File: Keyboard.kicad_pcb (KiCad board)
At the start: 2 copper layers, 231.8 x 98.9 mm, 153 parts, among them Q1 BSS138, Q2 BSS138, SW1 SW_Kailh_1u, SW10 SW_Kailh_1u, SW11 SW_Kailh_1u, SW12 SW_Kailh_1u, SW13 SW_Kailh_1u, SW14 SW_Kailh_1u, SW15 SW_Kailh_1u, SW16 SW_Kailh_1u, SW17 SW_Kailh_1u, SW18 SW_Kailh_1u, SW19 SW_Kailh_1u, SW2 SW_Kailh_1u, SW20 SW_Kailh_1u, SW21 SW_Kailh_1u, SW22 SW_Kailh_1u, SW23 SW_Kailh_1u, SW23_3u1 SW_Kailh_3u, SW24 SW_Kailh_1u, SW25 SW_Kailh_1u, SW26 SW_Kailh_1u, SW27 SW_Kailh_1u, SW28 SW_Kailh_1u, SW29 SW_Kailh_1u, SW3 SW_Kailh_1u, SW30 SW_Kailh_1u, SW31 SW_Kailh_1u, SW32 SW_Kailh_1u, SW33 SW_Kailh_1u, SW34 SW_Kailh_1u, SW35 SW_Kailh_1u, SW36 SW_Kailh_1u, SW37 SW_Kailh_1u, SW38 SW_Kailh_1u, SW39 SW_Kailh_1u, SW4 SW_Kailh_1u, SW40 SW_Kailh_1u, SW41 SW_Kailh_1u, SW42 SW_Kailh_1u, SW43 SW_Kailh_1u, SW44 SW_Kailh_1u, SW45 SW_Kailh_1u, SW5 SW_Kailh_1u, SW6 SW_Kailh_1u, SW7 SW_Kailh_1u, SW8 SW_Kailh_1u, SW9 SW_Kailh_1u, U1 PCAL6416APW, U2 Seeed Studio XIAO SAMD21, U3 NSI50350ADT4G

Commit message: rev 1.2
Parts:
- D1, D10, D11, D12, D13, D14, D15, D16, D17, D18, D19, D2, D20, D21, D22, D23, D24, D25, D26, D27, D28, D29, D3, D30, D31, D32, D33, D34, D35, D36, D37, D38, D39, D4, D40, D41, D42, D43, D44, D45, D46, D5, D6, D7, D8, D9: value 1N4148 -> 1N4148W; footprint Diode_SMD:D_1206_3216Metric_Pad1.42x1.75mm_HandSolder -> Diode_SMD:D_SOD-123
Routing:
- added copper zone on B.Cu, net GND
- added copper zone on F.Cu, net GND

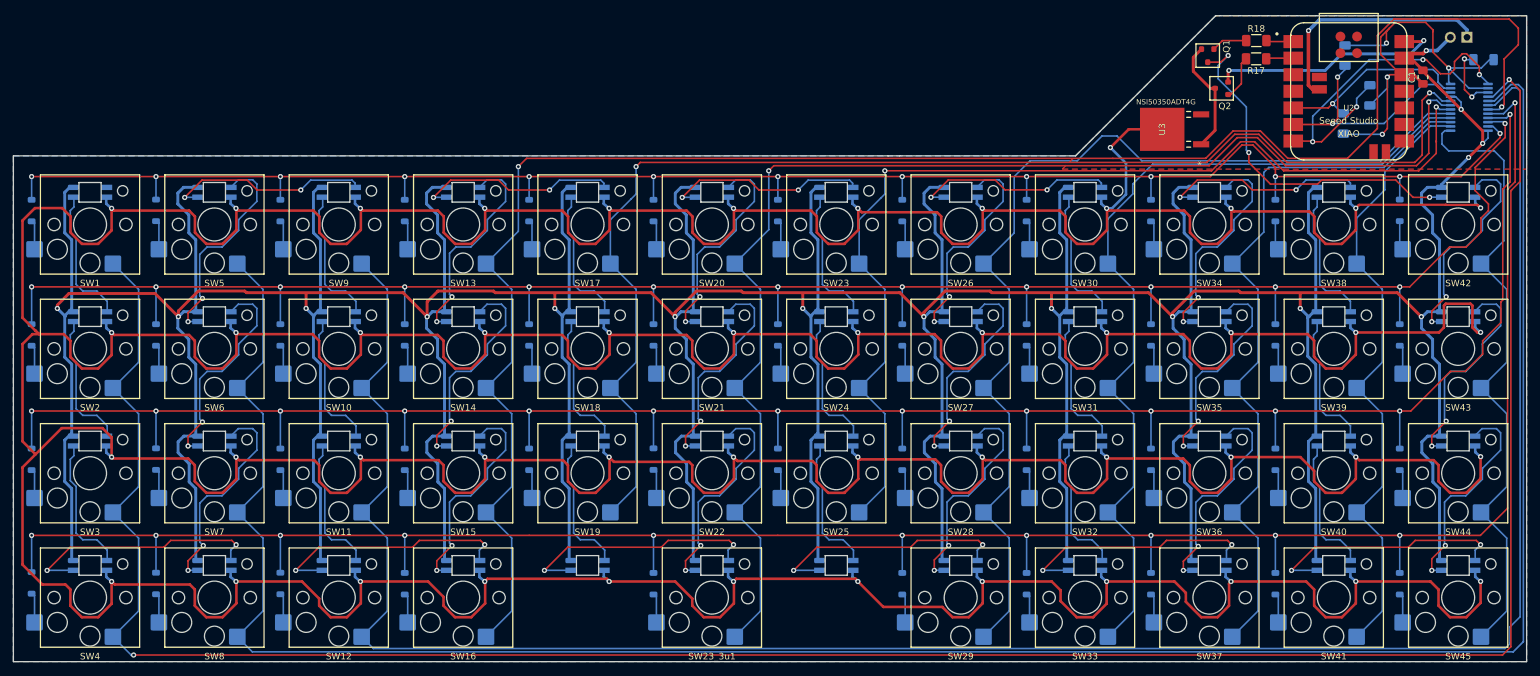
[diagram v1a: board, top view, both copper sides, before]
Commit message: rounded corners, replaced current reg with fuse
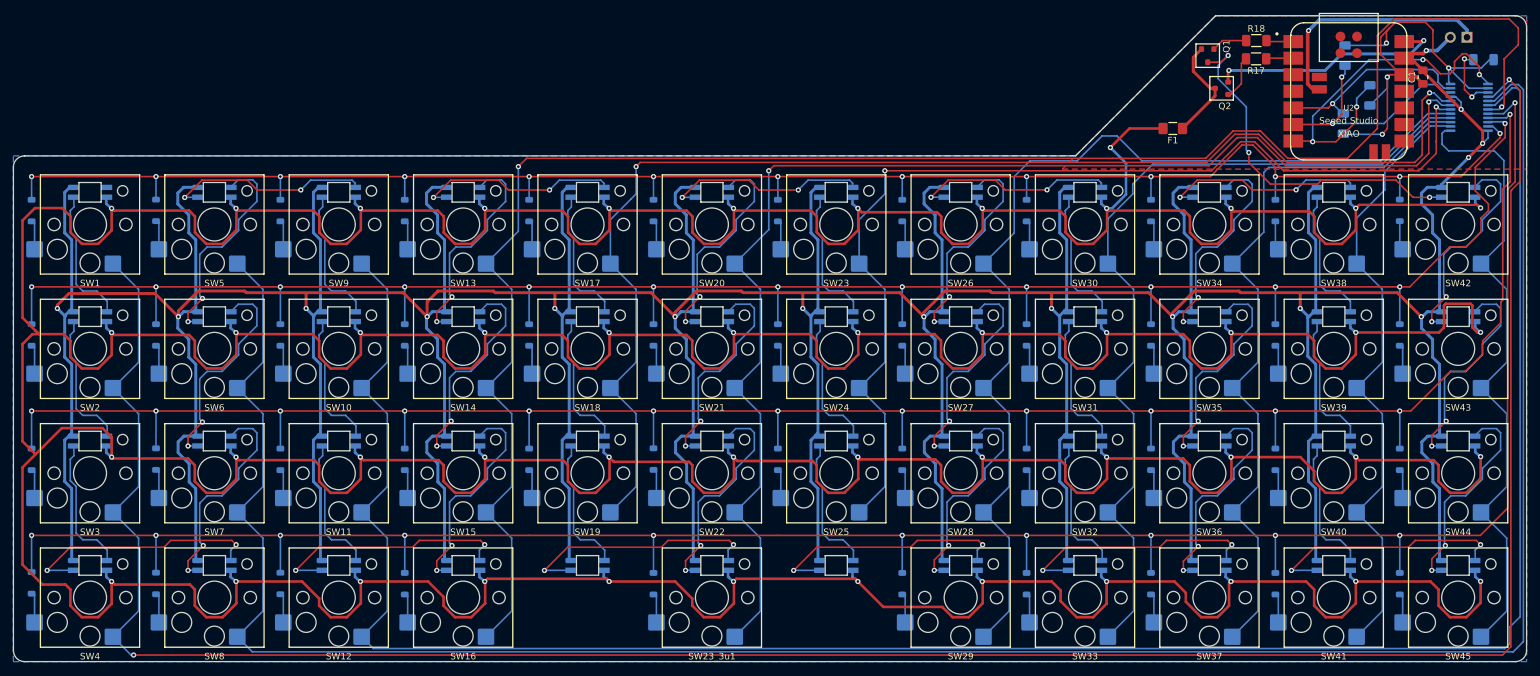
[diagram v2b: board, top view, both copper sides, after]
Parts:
- removed U3: NSI50350ADT4G, footprints:NSI50350ADT4G
- added F1: 500mA, Fuse:Fuse_1206_3216Metric_Pad1.42x1.75mm_HandSolder, F.Cu at (200.4, 55.5)
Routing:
- net INT: track 56.0 -> 57.3 mm
- net Net-(Q1-S): track 17.8 -> 16.6 mm
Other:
- outline, holes or cut-outs redrawn

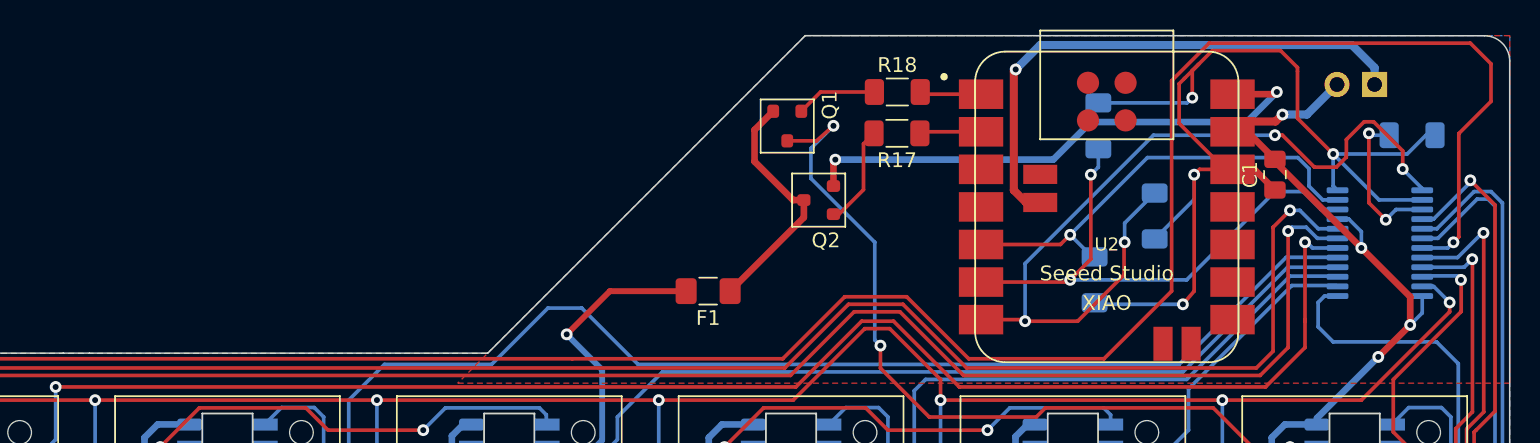
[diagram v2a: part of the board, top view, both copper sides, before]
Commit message: changed led mosfet and resistors
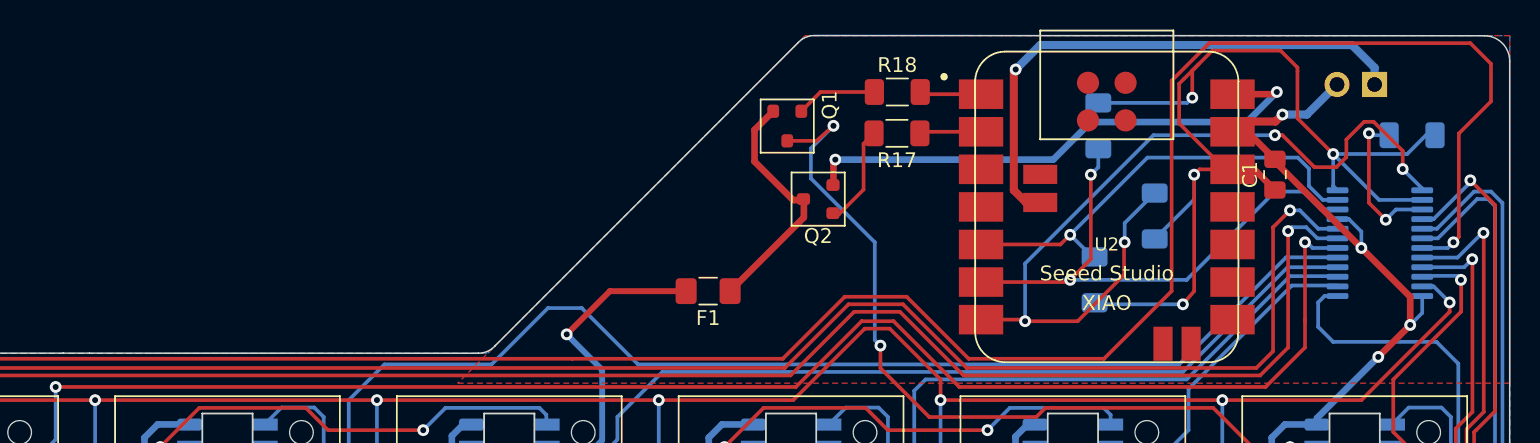
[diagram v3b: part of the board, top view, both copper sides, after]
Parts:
- Q2: value BSS138 -> DMG3402L
- R17, R18: value 10k -> 1k
- moved Q2 0.07 mm to (207.9, 49.3)
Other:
- outline, holes or cut-outs redrawn
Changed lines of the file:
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@@
         (effects (font (size 1 1) (thickness 0.15)))
     )
-    (fp_text value "10k" (at 0 1.82) (layer "F.Fab")
+    (fp_text value "1k" (at 0 1.82) (layer "F.Fab")
         (effects (font (size 1 1) (thickness 0.15)))
     )
@@
       (net 1 "Net-(BT1-+)") (pinfunction "BAT+") (pintype "input"))
   )
+  (footprint "PCM_Package_TO_SOT_SMD_AKL:SOT-23" (layer "F.Cu")
+    (at 207.883 49.276 180)
+    (descr "SOT-23, Standard, Alternate KiCad Library")
+    (tags "SOT-23")
+    (property "Sheetfile" "rgb.kicad_sch")
+    (property "Sheetname" "RGB LEDs")
+    (property "ki_description" "SOT-23 N-MOSFET enchancement mode transistor, 30V, 4A, 1.4W, Alternate KiCAD Library")
+    (property "ki_keywords" "enchancement mosfet nmosfet n-mosfet nmos n-mos emos emosfet DMG3402L")
+    (attr smd)
+    (fp_text reference "Q2" (at 0 -2.5) (layer "F.SilkS")
+        (effects (font (size 1 1) (thickness 0.15)))
+    )
+    (fp_text value "DMG3402L" (at 0 2.5) (layer "F.Fab") hide
+        (effects (font (size 1 1) (thickness 0.15)))
+    )
+    (fp_text user "${REFERENCE}" (at 0 0 90) (layer "F.Fab")
+        (effects (font (size 0.5 0.5) (thickness 0.075)))
+    )
+    (fp_line (start -1.8 -1.8) (end -1.8 1.8)
+      (stroke (width 0.12) (type solid)) (layer "F.SilkS"))
+    (fp_line (start -1.8 1.8) (end 1.8 1.8)
+      (stroke (width 0.12) (type solid)) (layer "F.SilkS"))
+    (fp_line (start 1.8 -1.8) (end -1.8 -1.8)
+      (stroke (width 0.12) (type solid)) (layer "F.SilkS"))
+    (fp_line (start 1.8 1.8) (end 1.8 -1.8)
+      (stroke (width 0.12) (type solid)) (layer "F.SilkS"))
+    (fp_line (start -1.7 -1.75) (end 1.7 -1.75)
+      (stroke (width 0.05) (type solid)) (layer "F.CrtYd"))
+    (fp_line (start -1.7 1.75) (end -1.7 -1.75)
+      (stroke (width 0.05) (type solid)) (layer "F.CrtYd"))
+    (fp_line (start 1.7 -1.75) (end 1.7 1.75)
+      (stroke (width 0.05) (type solid)) (layer "F.CrtYd"))
+    (fp_line (start 1.7 1.75) (end -1.7 1.75)
+      (stroke (width 0.05) (type solid)) (layer "F.CrtYd"))
+    (fp_line (start -1.3 -1.2) (end -1.3 -0.7)
+      (stroke (width 0.1) (type solid)) (layer "F.Fab"))
+    (fp_line (start -1.3 -0.7) (end -0.7 -0.7)
+      (stroke (width 0.1) (type solid)) (layer "F.Fab"))
+    (fp_line (start -1.3 0.7) (end -1.3 1.2)
+      (stroke (width 0.1) (type solid)) (layer "F.Fab"))
+    (fp_line (start -1.3 1.2) (end -0.7 1.2)
+      (stroke (width 0.1) (type solid)) (layer "F.Fab"))
+    (fp_line (start -0.7 -1.52) (end -0.7 1.5)
+      (stroke (width 0.1) (type solid)) (layer "F.Fab"))
+    (fp_line (start -0.7 -1.52) (end 0.7 -1.52)
+      (stroke (width 0.1) (type solid)) (layer "F.Fab"))
+    (fp_line (start -0.7 -1.2) (end -1.3 -1.2)
+      (stroke (width 0.1) (type solid)) (layer "F.Fab"))
+    (fp_line (start -0.7 0.7) (end -1.3 0.7)
+      (stroke (width 0.1) (type solid)) (layer "F.Fab"))
+    (fp_line (start -0.7 1.52) (end 0.7 1.52)
+      (stroke (width 0.1) (type solid)) (layer "F.Fab"))
+    (fp_line (start 0.7 -1.52) (end 0.7 1.52)
+      (stroke (width 0.1) (type solid)) (layer "F.Fab"))
+    (fp_line (start 0.7 0.25) (end 1.3 0.25)
+      (stroke (width 0.1) (type solid)) (layer "F.Fab"))
+    (fp_line (start 1.3 -0.25) (end 0.7 -0.25)
+      (stroke (width 0.1) (type solid)) (layer "F.Fab"))
+    (fp_line (start 1.3 0.25) (end 1.3 -0.25)
+      (stroke (width 0.1) (type solid)) (layer "F.Fab"))
+    (pad "1" smd roundrect (at -1 -0.95 180) (size 0.9 0.8) (layers "F.Cu" "F.Paste" "F.Mask") (roundrect_rratio 0.25)
+      (net 134 "Net-(Q2-G)") (pinfunction "G") (pintype "input"))
+    (pad "2" smd roundrect (at -1 0.95 180) (size 0.9 0.8) (layers "F.Cu" "F.Paste" "F.Mask") (roundrect_rratio 0.25)
+      (net 76 "VCC_5V") (pinfunction "S") (pintype "passive"))
+    (pad "3" smd roundrect (at 1 0 180) (size 0.9 0.8) (layers "F.Cu" "F.Paste" "F.Mask") (roundrect_rratio 0.25)
+      (net 133 "Net-(Q1-S)") (pinfunction "D") (pintype "passive"))
+    (model "${KICAD6_3DMODEL_DIR}/Package_TO_SOT_SMD.3dshapes/SOT-23.wrl"
+      (offset (xyz 0 0 0))
+      (scale (xyz 1 1 1))
+      (rotate (xyz 0 0 0))
+    )
+  )
   (footprint "PCM_Switch_Keyboard_Hotswap_Kailh:SW_Hotswap_Kailh_Choc_V1V2_1.00u" (layer "F.Cu")
     (at 91.75 70.2 180)
@@
         (effects (font (size 1 1) (thickness 0.15)))
     )
-    (fp_text value "10k" (at 0 1.82) (layer "F.Fab")
+    (fp_text value "1k" (at 0 1.82) (layer "F.Fab")
         (effects (font (size 1 1) (thickness 0.15)))
     )
@@
     )
   )
-  (footprint "PCM_Package_TO_SOT_SMD_AKL:SOT-23" (layer "F.Cu")
-    (at 207.915 49.342 180)
-    (descr "SOT-23, Standard, Alternate KiCad Library")
-    (tags "SOT-23")
-    (property "Sheetfile" "rgb.kicad_sch")
-    (property "Sheetname" "RGB LEDs")
-    (property "ki_description" "SOT-23 N-MOSFET enchancement mode transistor, 50V, 200mA, 300mW, Alternate KiCAD Library")
-    (property "ki_keywords" "enchancement mosfet nmosfet n-mosfet nmos n-mos emos emosfet BSS138")
-    (attr smd)
-    (fp_text reference "Q2" (at -0.492 -2.728) (layer "F.SilkS")
-        (effects (font (size 1 1) (thickness 0.15)))
-    )
-    (fp_text value "BSS138" (at 0 2.5) (layer "F.Fab") hide
-        (effects (font (size 1 1) (thickness 0.15)))
-    )
-    (fp_text user "${REFERENCE}" (at 0 0 90) (layer "F.Fab")
-        (effects (font (size 0.5 0.5) (thickness 0.075)))
-    )
-    (fp_line (start -1.8 -1.8) (end -1.8 1.8)
-      (stroke (width 0.12) (type solid)) (layer "F.SilkS"))
-    (fp_line (start -1.8 1.8) (end 1.8 1.8)
-      (stroke (width 0.12) (type solid)) (layer "F.SilkS"))
-    (fp_line (start 1.8 -1.8) (end -1.8 -1.8)
-      (stroke (width 0.12) (type solid)) (layer "F.SilkS"))
-    (fp_line (start 1.8 1.8) (end 1.8 -1.8)
-      (stroke (width 0.12) (type solid)) (layer "F.SilkS"))
-    (fp_line (start -1.7 -1.75) (end 1.7 -1.75)
-      (stroke (width 0.05) (type solid)) (layer "F.CrtYd"))
-    (fp_line (start -1.7 1.75) (end -1.7 -1.75)
-      (stroke (width 0.05) (type solid)) (layer "F.CrtYd"))
-    (fp_line (start 1.7 -1.75) (end 1.7 1.75)
-      (stroke (width 0.05) (type solid)) (layer "F.CrtYd"))
-    (fp_line (start 1.7 1.75) (end -1.7 1.75)
-      (stroke (width 0.05) (type solid)) (layer "F.CrtYd"))
-    (fp_line (start -1.3 -1.2) (end -1.3 -0.7)
-      (stroke (width 0.1) (type solid)) (layer "F.Fab"))
-    (fp_line (start -1.3 -0.7) (end -0.7 -0.7)
-      (stroke (width 0.1) (type solid)) (layer "F.Fab"))
-    (fp_line (start -1.3 0.7) (end -1.3 1.2)
-      (stroke (width 0.1) (type solid)) (layer "F.Fab"))
-    (fp_line (start -1.3 1.2) (end -0.7 1.2)
-      (stroke (width 0.1) (type solid)) (layer "F.Fab"))
-    (fp_line (start -0.7 -1.52) (end -0.7 1.5)
-      (stroke (width 0.1) (type solid)) (layer "F.Fab"))
-    (fp_line (start -0.7 -1.52) (end 0.7 -1.52)
-      (stroke (width 0.1) (type solid)) (layer "F.Fab"))
-    (fp_line (start -0.7 -1.2) (end -1.3 -1.2)
-      (stroke (width 0.1) (type solid)) (layer "F.Fab"))
-    (fp_line (start -0.7 0.7) (end -1.3 0.7)
-      (stroke (width 0.1) (type solid)) (layer "F.Fab"))
-    (fp_line (start -0.7 1.52) (end 0.7 1.52)
-      (stroke (width 0.1) (type solid)) (layer "F.Fab"))
-    (fp_line (start 0.7 -1.52) (end 0.7 1.52)
-      (stroke (width 0.1) (type solid)) (layer "F.Fab"))
-    (fp_line (start 0.7 0.25) (end 1.3 0.25)
-      (stroke (width 0.1) (type solid)) (layer "F.Fab"))
-    (fp_line (start 1.3 -0.25) (end 0.7 -0.25)
-      (stroke (width 0.1) (type solid)) (layer "F.Fab"))
-    (fp_line (start 1.3 0.25) (end 1.3 -0.25)
-      (stroke (width 0.1) (type solid)) (layer "F.Fab"))
-    (pad "1" smd roundrect (at -1 -0.95 180) (size 0.9 0.8) (layers "F.Cu" "F.Paste" "F.Mask") (roundrect_rratio 0.25)
-      (net 134 "Net-(Q2-G)") (pinfunction "G") (pintype "input"))
-    (pad "2" smd roundrect (at -1 0.95 180) (size 0.9 0.8) (layers "F.Cu" "F.Paste" "F.Mask") (roundrect_rratio 0.25)
-      (net 76 "VCC_5V") (pinfunction "S") (pintype "passive"))
-    (pad "3" smd roundrect (at 1 0 180) (size 0.9 0.8) (layers "F.Cu" "F.Paste" "F.Mask") (roundrect_rratio 0.25)
-      (net 133 "Net-(Q1-S)") (pinfunction "D") (pintype "passive"))
-    (model "${KICAD6_3DMODEL_DIR}/Package_TO_SOT_SMD.3dshapes/SOT-23.wrl"
-      (offset (xyz 0 0 0))
-      (scale (xyz 1 1 1))
-      (rotate (xyz 0 0 0))
-    )
-  )
   (footprint "PCM_Switch_Keyboard_Hotswap_Kailh:SW_Hotswap_Kailh_Choc_V1V2_1.00u" (layer "F.Cu")
     (at 53.65 108.3 180)
@@
   (gr_arc (start 254.62744 135.44383) (mid 254.127 136.652) (end 252.91883 137.15244)
     (stroke (width 0.1) (type default)) (layer "Edge.Cuts"))
-  (gr_line (start 207.01 38.227) (end 252.91883 38.23456)
+  (gr_line (start 207.63648 38.219791) (end 252.91883 38.23456)
     (stroke (width 0.1) (type default)) (layer "Edge.Cuts"))
-  (gr_line (start 158.623 59.69) (end 185.547 59.69)
+  (gr_line (start 158.623 59.69) (end 184.912 59.695282)
     (stroke (width 0.1) (type default)) (layer "Edge.Cuts"))
   (gr_arc (start 22.86756 61.40617) (mid 23.368 60.198) (end 24.57617 59.69756)
@@
   (gr_line (start 22.86756 135.44383) (end 22.86756 61.40617)
     (stroke (width 0.1) (type default)) (layer "Edge.Cuts"))
-  (gr_line (start 185.547 59.69) (end 207.01 38.227)
+  (gr_line (start 186.055 59.182) (end 206.49348 38.733073)
+    (stroke (width 0.1) (type default)) (layer "Edge.Cuts"))
+  (gr_arc (start 186.055 59.182) (mid 185.53848 59.561073) (end 184.912 59.695282)
+    (stroke (width 0.1) (type default)) (layer "Edge.Cuts"))
+  (gr_arc (start 206.49348 38.733073) (mid 207.01 38.354) (end 207.63648 38.219791)
     (stroke (width 0.1) (type default)) (layer "Edge.Cuts"))
   (segment (start 221.107 40.64) (end 221.234 40.513) (width 0.55) (layer "F.Cu") (net 1))
